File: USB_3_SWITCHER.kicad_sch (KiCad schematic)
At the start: 0 parts

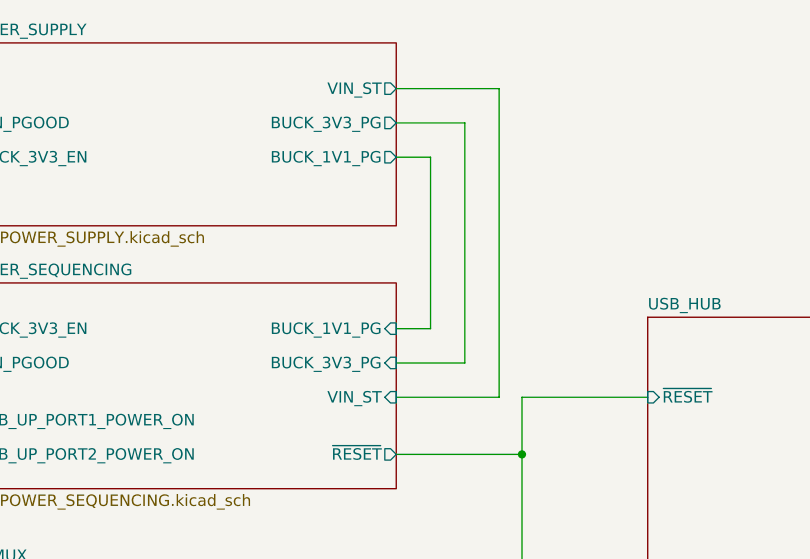
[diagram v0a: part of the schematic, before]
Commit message: Power In Circuitry extended for more current
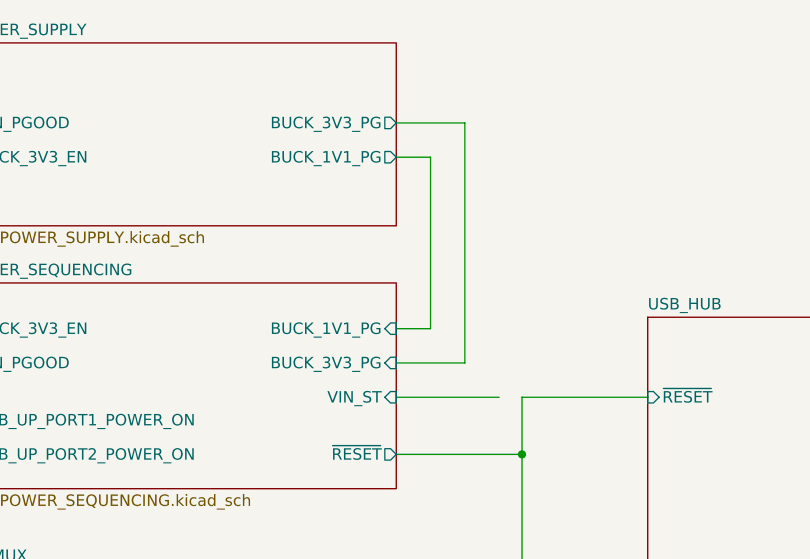
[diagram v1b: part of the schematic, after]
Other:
- sheet POWER_SUPPLY ports: added none; removed VIN_ST
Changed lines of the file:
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@@
-	(wire
-		(pts
-			(xy 185.42 35.56) (xy 185.42 69.85)
-		)
-		(stroke
-			(width 0)
-			(type default)
-		)
-	)
 	(wire
 		(pts
@@
 		(pts
 			(xy 262.89 72.39) (xy 285.75 72.39)
-		)
-		(stroke
-			(width 0)
-			(type default)
-		)
-	)
-	(wire
-		(pts
-			(xy 173.99 35.56) (xy 185.42 35.56)
 		)
 		(stroke
@@
 			(effects
 				(font
-					(size 1.27 1.27)
-				)
-				(justify right)
-			)
-		)
-		(pin "VIN_ST" output
-			(at 173.99 35.56 0)
-			(effects
-				(font

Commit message: Restored
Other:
- sheet POWER_SEQUENCING ports: added none; removed VIN_ST
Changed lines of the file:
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@@
-	(wire
-		(pts
-			(xy 185.42 69.85) (xy 173.99 69.85)
-		)
-		(stroke
-			(width 0)
-			(type default)
-		)
-	)
 	(wire
 		(pts
@@
 			(effects
 				(font
-					(size 1.27 1.27)
-				)
-				(justify right)
-			)
-		)
-		(pin "VIN_ST" input
-			(at 173.99 69.85 0)
-			(effects
-				(font
